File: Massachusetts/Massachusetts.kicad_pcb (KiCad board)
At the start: 2 copper layers, 1 part

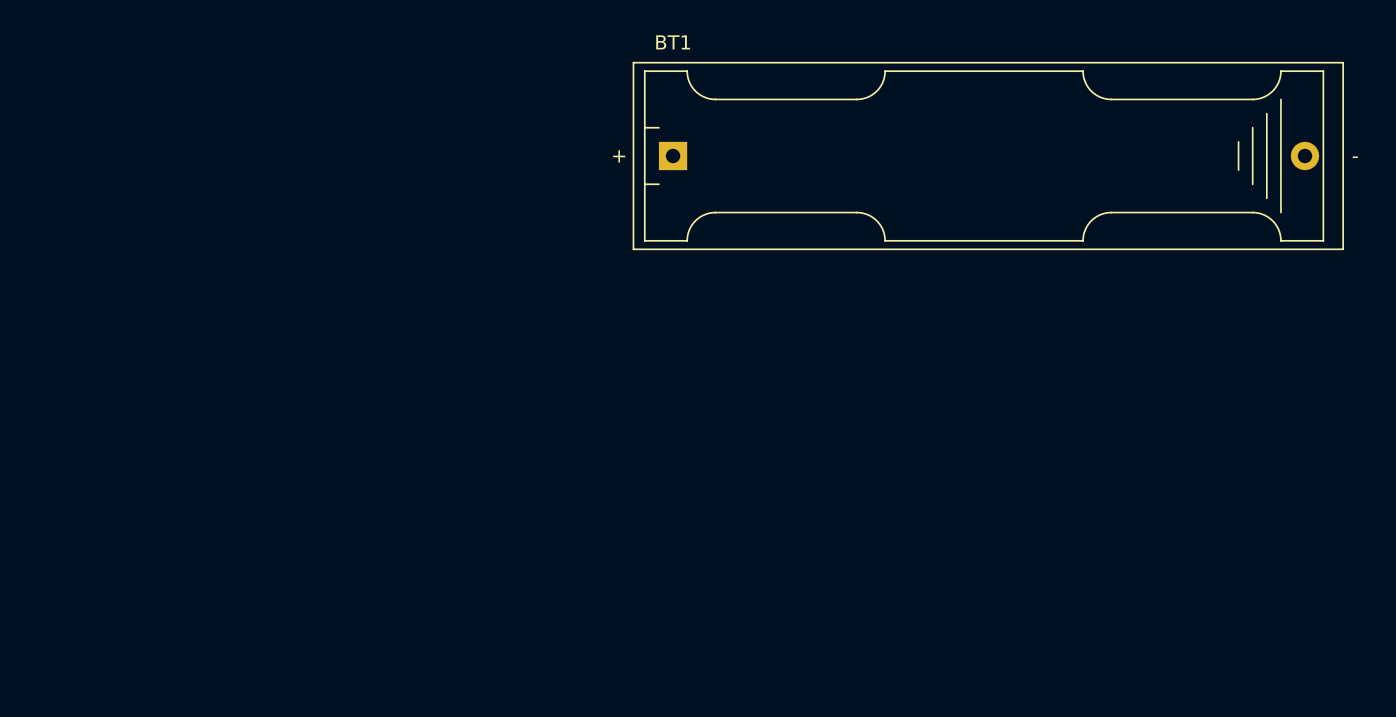
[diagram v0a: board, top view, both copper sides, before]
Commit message: linked schematic symbols to footprints
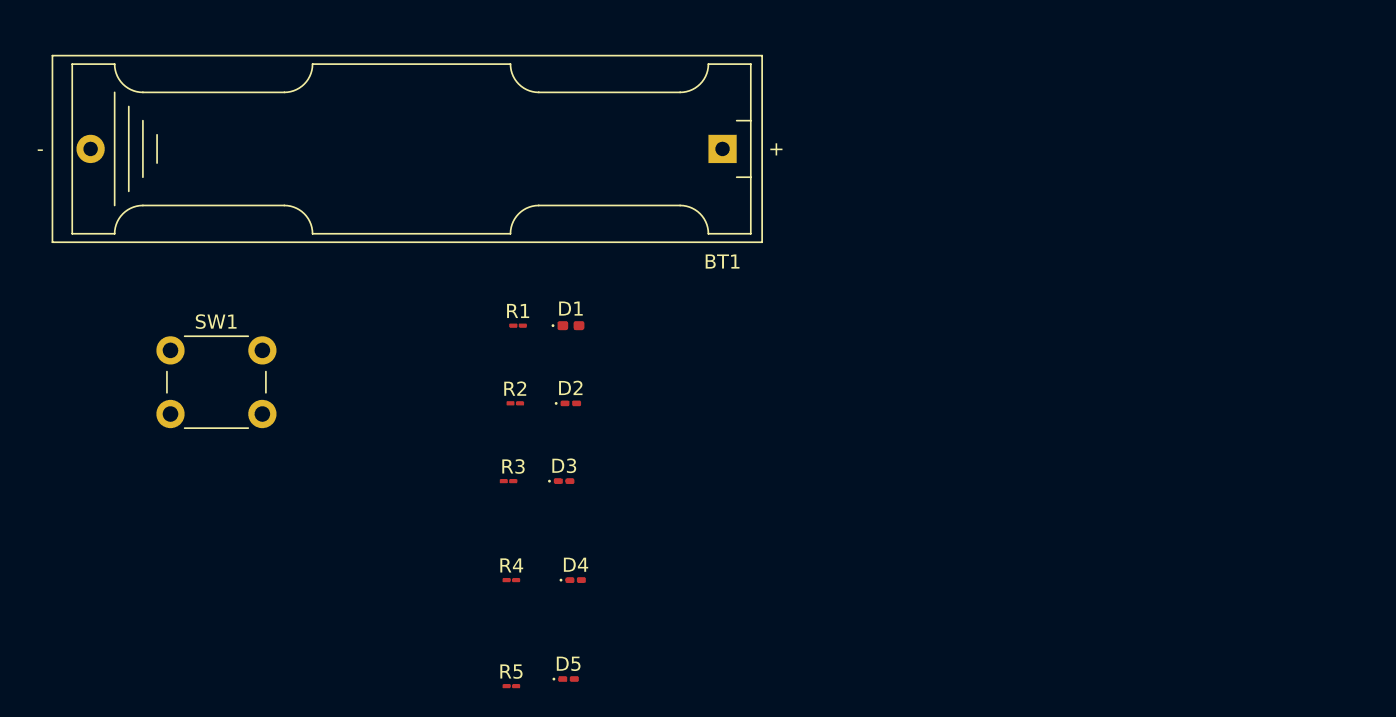
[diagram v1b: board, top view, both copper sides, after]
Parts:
- added D1: LED, LED_SMD:LED_0402_1005Metric_Pad0.77x0.64mm_HandSolder, F.Cu at (20.1, 59.5)
- added D2: LED, LED_SMD:LED_0201_0603Metric_Pad0.64x0.40mm_HandSolder, F.Cu at (20.1, 65.0)
- added D3: LED, LED_SMD:LED_0201_0603Metric_Pad0.64x0.40mm_HandSolder, F.Cu at (19.6, 70.5)
- added D4: LED, LED_SMD:LED_0201_0603Metric_Pad0.64x0.40mm_HandSolder, F.Cu at (20.4, 77.5)
- added D5: LED, LED_SMD:LED_0201_0603Metric_Pad0.64x0.40mm_HandSolder, F.Cu at (19.9, 84.5)
- added R1: R, Resistor_SMD:R_01005_0402Metric_Pad0.57x0.30mm_HandSolder, F.Cu at (16.3, 59.5)
- added R2: R, Resistor_SMD:R_01005_0402Metric_Pad0.57x0.30mm_HandSolder, F.Cu at (16.1, 65.0)
- added R3: R, Resistor_SMD:R_01005_0402Metric_Pad0.57x0.30mm_HandSolder, F.Cu at (15.7, 70.5)
- added R4: R, Resistor_SMD:R_01005_0402Metric_Pad0.57x0.30mm_HandSolder, F.Cu at (15.9, 77.5)
- added R5: R, Resistor_SMD:R_01005_0402Metric_Pad0.57x0.30mm_HandSolder, F.Cu at (15.9, 85.0)
- added SW1: SW_Push, Button_Switch_THT:SW_PUSH_6mm_H4.3mm, F.Cu at (-8.25, 61.2)
- moved BT1 3.54 mm to (30.8, 47.0), turned to 180 degrees

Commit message: Added touch slider
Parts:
- removed SW1: SW_Push, Button_Switch_THT:SW_PUSH_6mm_H4.3mm
- added G***: LOGO, Massachusetts:Mass_Outline, F.Cu at (321.1, 206.8)
- added SW2: ~, touchswitch:Touch_Switch, F.Cu at (152.0, 131.5)
- BT1: footprint Battery:BatteryHolder_Keystone_2466_1xAAA -> Battery:BatteryHolder_Keystone_3034_1x20mm; moved to B.Cu
- D1: footprint LED_SMD:LED_0402_1005Metric_Pad0.77x0.64mm_HandSolder -> LED_SMD:LED_0603_1608Metric_Pad1.05x0.95mm_HandSolder
- D2, D3, D4, D5: footprint LED_SMD:LED_0201_0603Metric_Pad0.64x0.40mm_HandSolder -> LED_SMD:LED_0603_1608Metric_Pad1.05x0.95mm_HandSolder
- R1, R2, R3, R4, R5: footprint Resistor_SMD:R_01005_0402Metric_Pad0.57x0.30mm_HandSolder -> Resistor_SMD:R_0603_1608Metric_Pad0.98x0.95mm_HandSolder; moved to B.Cu
- moved BT1 173.9 mm to (190.2, 116.6), turned to 90 degrees
- moved R3 155.2 mm to (165.7, 110.5), turned to 180 degrees
- moved R4 148.8 mm to (162.1, 105.1), turned to -90 degrees
- moved D4 141.9 mm to (158.9, 108.3)
- moved R1 126.0 mm to (131.9, 109.7)
- moved D3 125.0 mm to (139.1, 107.2)
- moved R2 124.9 mm to (136.3, 99.1)
- moved D2 122.4 mm to (136.5, 102.8)
- moved D1 120.9 mm to (132.4, 104.2)
- moved D5 119.9 mm to (135.7, 115.6), turned to 180 degrees
- moved R5 118.7 mm to (130.6, 115.5), turned to -90 degrees
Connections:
- net Net-(BT1-+) renamed VCC
- BT1 pad 2: Net-(BT1--) -> GND
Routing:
- net VCC: track 0.00 -> 132.5 mm
- net Net-(D1-K): track 0.00 -> 92.7 mm, vias 0 -> 8
- net GND: track 0.00 -> 41.4 mm, vias 0 -> 1
- net Net-(D3-A): track 0.00 -> 26.8 mm, vias 0 -> 1
- net Net-(D1-A): track 0.00 -> 5.70 mm, vias 0 -> 1
- net Net-(D5-A): track 0.00 -> 5.67 mm, vias 0 -> 1
- net Net-(D4-A): track 0.00 -> 4.03 mm, vias 0 -> 1
- net Net-(D2-A): track 0.00 -> 3.79 mm, vias 0 -> 1
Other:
- board outline added: 81 x 50.6 mm
- board text added: "Crum Hill"
- board text added: "Mount Greylock"
- board text added: "Round Top Hill"
- board text added: "Top 5 Massachusetts County High Points"
- board text added: "Wachusett Mountain"
- board text added: "West Mountain"

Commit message: V1 ordered
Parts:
- removed SW2: ~, touchswitch:Touch_Switch
- added S1: TL3315NF160Q, TL3315NF160Q:SW_TL3315NF160Q, F.Cu at (142.4, 130.6)
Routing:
- net GND: track 41.4 -> 88.0 mm, vias 1 -> 2
- net Net-(D1-K): track 92.7 -> 72.8 mm, vias 8 -> 9

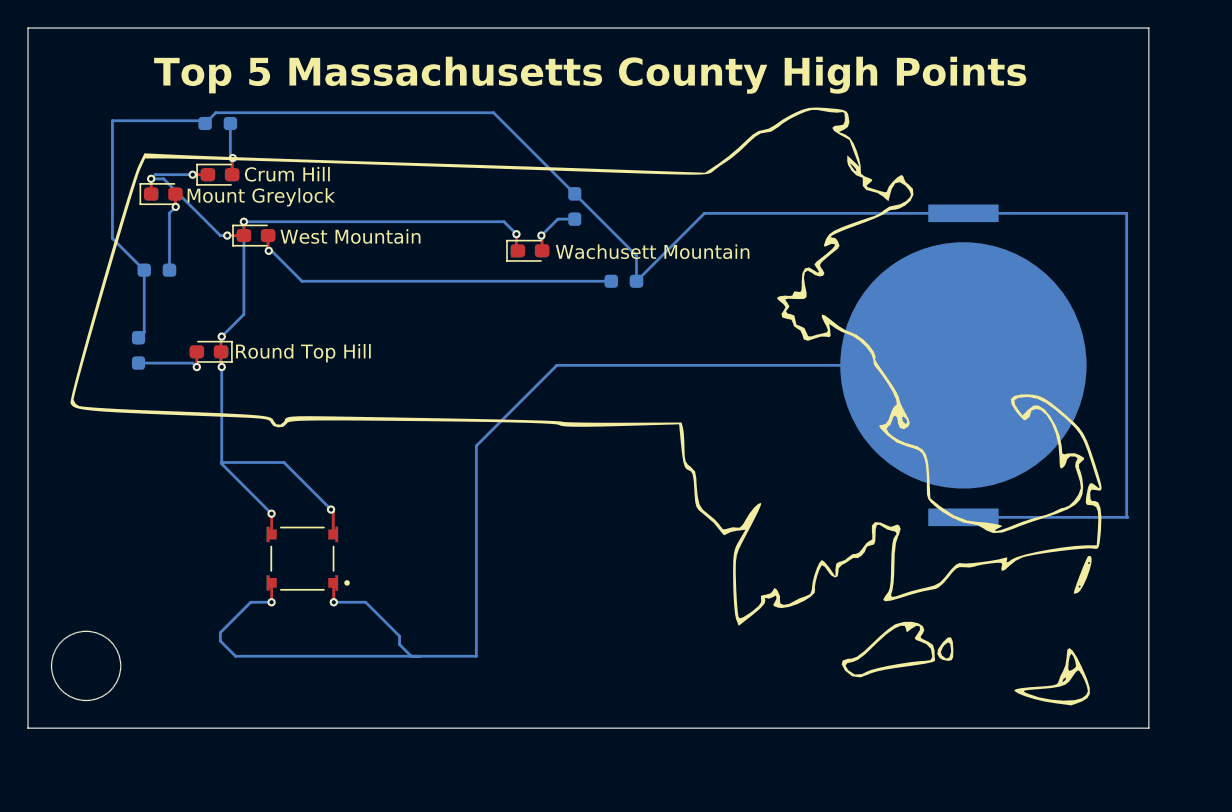
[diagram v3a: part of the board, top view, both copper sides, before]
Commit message: centered battery
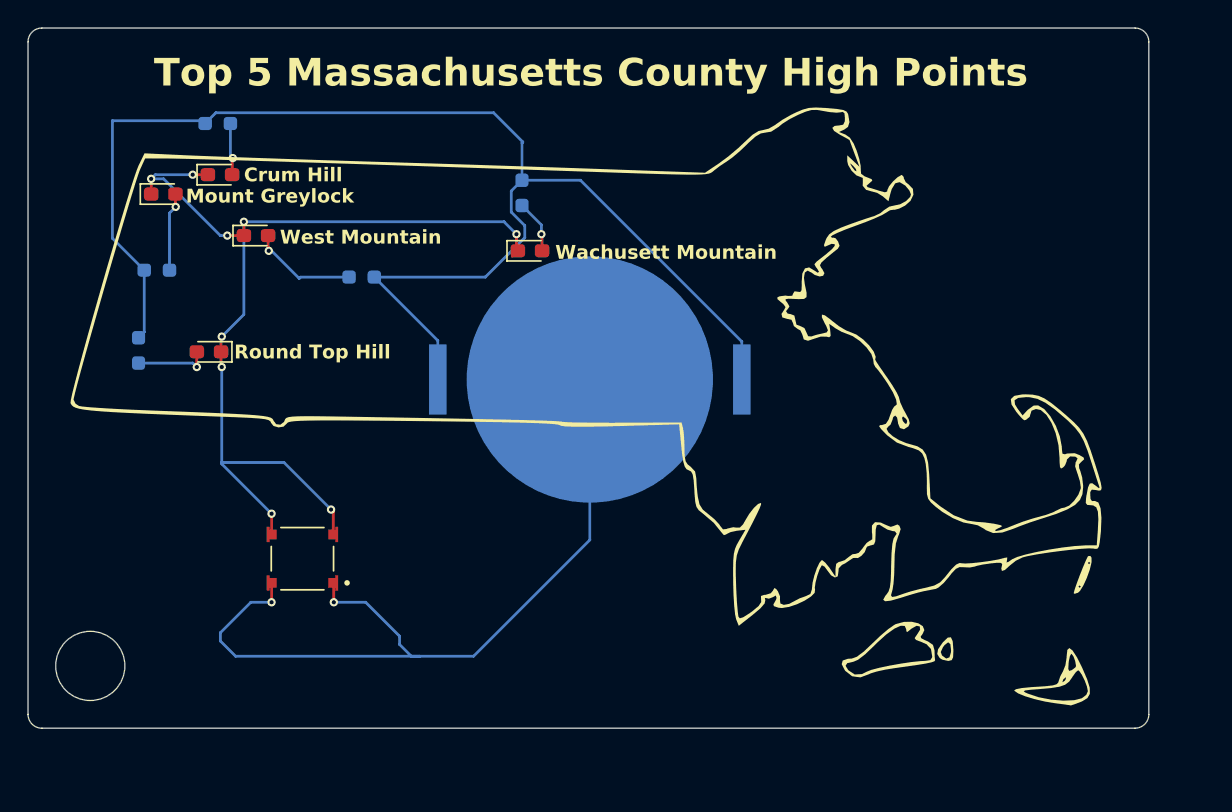
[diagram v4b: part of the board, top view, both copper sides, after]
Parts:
- moved BT1 27.0 mm to (163.2, 117.6), turned to 180 degrees
- moved R3 19.0 mm to (146.7, 110.2)
- moved R4 3.94 mm to (158.3, 104.1)
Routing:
- net VCC: track 132.5 -> 100.2 mm
- net GND: track 88.0 -> 58.4 mm
- net Net-(D3-A): track 26.8 -> 7.79 mm
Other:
- outline, holes or cut-outs redrawn
